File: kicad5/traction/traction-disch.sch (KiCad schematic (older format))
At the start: 26 parts

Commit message: Rev A.7: review round 7 response (RR01-RR10, A6-R01-R14) + cross-check
Two independent rechecks of c963794 were verified finding by finding and
classified in docs/review-A7-disposition.md (+ .csv): 17 confirmed and fixed,
1 spec gap closed, 3 firmware handled, 3 already-tracked release gates. Two
further defects were self-found (N10, N11).

Safety logic (control card):
- 74LVC3G17-Q100 Schmitt buffer between the RC timing nodes (clear one-shot,
  soft-off delay) and the LVC inputs they drove at 14,000-63,500 ns/V. The
  FS0B line goes through it too; a 100 k pull-down makes a dead buffer
  force DRV_EN low.
- FS0B/FS1B pull-ups 1 k -> 5.1 k (FS1B inside its 2 mA V_OL point).
- FAULT_OUT made sink-only (BAT46): a grounded vehicle wire can no longer
  preset ASC. A KL30 short is clamped at the latch.
- DRV_EN and ASC_CMD read-backs to the MCU for a boot self-test.
- Latches moved to Nexperia 74LVC1G74DC-Q100 (the TI part is not Q100).
- CCLR changed to C0G.

ASC entry is now break-before-make:
- A 12 nF delay (+ fast-release diode) holds the LS ASC off >= 3.4 us.
- MCU path: HS off via the eFlexPWM fault, then PWM-ASC with EN high.
- MCU-dead path: FS0B, then the delayed ASC.
- EN is never dropped for ASC: NSI6611 DS 8.12 honours DESAT over ASC only
  with EN high. The first draft's DASC diode did drop it and was removed
  after the cross-check.
- 1 k series resistor at each LS ASC pin.
- ASC opto LED resistor 470 -> 270 R (TLP152 I_FLH max 7.5 mA).

Gate supply:
- The flyback FB divider senses its own aux rectifier, so the start feed
  can no longer lock gate power out at high KL30.
- 52.3k/15k: VCC2 15.4 V nominal, 13.54-16.7 V corners.
- Boost output capacitors 25 V -> 50 V.

Models and checkers:
- IGBT and diode share the coldplate term.
- Flyback bank inductance corrected.
- SC soft-off checked at both I_STO corners (release gate).
- FW-06 as a measured budget: 15.6 us + 7.0 us all-off -> 905/542 V.
- bom-gen preflight and a JSWD pin-count check (Samtec 10-pin).
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
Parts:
- removed JCTL: HDR-1x4-2.54, HDR1x4, symbol traction-r1:HDR-1x4-2.54
- removed JDCN, JDCP: STUD-M6, StudM6, symbol traction-r1:TERM_1
- removed RBLD1, RBLD10, RBLD11, RBLD12, RBLD2, RBLD3, RBLD4, RBLD5: 22k, R2512, symbol traction-r1:R
- added CQD: 100nF, C0603, symbol traction-r1:C
- added PSQD: QA01C-18, SIP7, symbol traction-r1:QA01C-18
- added QDIS: HCM75S12T4K3, TO247-4L, symbol traction-r1:HCM75S12T4K3
- added RDIS1, RDIS2, RDIS3, RDIS4: 470R, AxialWW10W, symbol traction-r1:R
- added RQDG: 47R, R0603, symbol traction-r1:R
- added RQDL: 470R, R0603, symbol traction-r1:R
- added RQDPD: 10k, R0603, symbol traction-r1:R
- added UQD: TLP152, SO6, symbol traction-r1:TLP152
- JCTL: renamed from RBLD6; value 22k -> HDR-1x4-2.54; footprint R2512 -> HDR1x4; symbol traction-r1:R -> traction-r1:HDR-1x4-2.54; MPN R2512-22k-2W -> HDR-1x4-2.54
- JDCN: renamed from RBLD7; value 22k -> STUD-M6; footprint R2512 -> StudM6; symbol traction-r1:R -> traction-r1:TERM_1; MPN R2512-22k-2W -> STUD-M6
- JDCP: renamed from RBLD8; value 22k -> STUD-M6; footprint R2512 -> StudM6; symbol traction-r1:R -> traction-r1:TERM_1; MPN R2512-22k-2W -> STUD-M6
- RBLD10: renamed from PSQD; value QA01C-18 -> 22k; footprint SIP7 -> R2512; symbol traction-r1:QA01C-18 -> traction-r1:R; MPN QA01C-18 -> R2512-22k-2W
- RBLD11: renamed from QDIS; value HCM75S12T4K3 -> 22k; footprint TO247-4L -> R2512; symbol traction-r1:HCM75S12T4K3 -> traction-r1:R; MPN HCM75S12T4K3 -> R2512-22k-2W
- RBLD12: renamed from UQD; value TLP152 -> 22k; footprint SO6 -> R2512; symbol traction-r1:TLP152 -> traction-r1:R; LCSC C17255258 -> CLASS; MPN TLP152 -> R2512-22k-2W
- RBLD2: renamed from CQD; value 100nF -> 22k; footprint C0603 -> R2512; symbol traction-r1:C -> traction-r1:R; MPN MLCC-100nF-25V -> R2512-22k-2W
- RBLD3: renamed from RDIS1; value 470R -> 22k; footprint AxialWW10W -> R2512; MPN WW-470R-10W-AX -> R2512-22k-2W
- RBLD4: renamed from RDIS2; value 470R -> 22k; footprint AxialWW10W -> R2512; MPN WW-470R-10W-AX -> R2512-22k-2W
- RBLD5: renamed from RDIS3; value 470R -> 22k; footprint AxialWW10W -> R2512; MPN WW-470R-10W-AX -> R2512-22k-2W
- RBLD6: renamed from RDIS4; value 470R -> 22k; footprint AxialWW10W -> R2512; MPN WW-470R-10W-AX -> R2512-22k-2W
- RBLD7: renamed from RQDG; value 47R -> 22k; footprint R0603 -> R2512; MPN R0603-47R -> R2512-22k-2W
- RBLD8: renamed from RQDL; value 470R -> 22k; footprint R0603 -> R2512; MPN R0603-470R -> R2512-22k-2W
- RBLD9: renamed from RQDPD; value 10k -> 22k; footprint R0603 -> R2512; MPN R0603-10k -> R2512-22k-2W
- renumbered RBLD9 to RBLD1
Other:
- note added: "220 kW pk Discharge (HV, bolt-on) - 3 of 4 · rev A.7 · 3 sections · 26 components"
- note removed: "220 kW pk Discharge (HV, bolt-on) - 3 of 4 · rev A.6 · 3 sections · 26 components"
- moved on the sheet: RBLD1, RBLD3, RBLD4, RBLD5, RBLD6, RBLD7, RBLD8, RBLD9
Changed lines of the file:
@@
 Title "Traction Inverter — Discharge board (bolt-on, XM3 pattern)"
 Date "2026-09-23"
-Rev "A.6"
+Rev "A.7"
 Comp "Traction Inverter 220 kW pk - Discharge (HV, bolt-on), sheet 3 of 4"
 Comment1 "Inverter = Power board + Cap bank busbar + bolt-on Discharge board (all HV) + Control card (LV); safe state holds with any link lost"
@@
 $EndDescr
 Text Notes 600 7600 0    60   ~ 12
-220 kW pk Discharge (HV, bolt-on) - 3 of 4   ·   rev A.6   ·   3 sections   ·   26 components
+220 kW pk Discharge (HV, bolt-on) - 3 of 4   ·   rev A.7   ·   3 sections   ·   26 components
 Text Notes 600 7900 0    50   ~ 0
 NET NAMING: U<ref>_<PIN> = node at that IC pin   ·   R<stem>_M = series-pair midpoint   ·   R<stem>_<nm> = tap between R<stem>n/m   ·   all others are explicit design nets   ·   same name on another sheet = same net, joined only at the named connector/stud/tab
@@
 $Comp
 L traction-r1:HDR-1x4-2.54 JCTL
-U 1 1 5E000142
+U 1 1 5E00014D
 P 9150 5850
 F 0 "JCTL" H 8750 5550 50  0000 R CNN
@@
 $Comp
 L traction-r1:TERM_1 JDCN
-U 1 1 5E000143
+U 1 1 5E00014E
 P 8800 5300
 F 0 "JDCN" H 8800 5140 50  0000 C CNN
@@
 $Comp
 L traction-r1:TERM_1 JDCP
-U 1 1 5E000144
+U 1 1 5E00014F
 P 8800 4900
 F 0 "JDCP" H 8800 4740 50  0000 C CNN
@@
 $Comp
 L traction-r1:R RBLD1
-U 1 1 5E000145
+U 1 1 5E000150
 P 8300 1150
 F 0 "RBLD1" H 8300 990 50  0000 C CNN
@@
 $Comp
 L traction-r1:R RBLD10
-U 1 1 5E000146
+U 1 1 5E000151
 P 9800 2350
 F 0 "RBLD10" H 9800 2190 50  0000 C CNN
@@
 $Comp
 L traction-r1:R RBLD11
-U 1 1 5E000147
+U 1 1 5E000152
 P 9800 2750
 F 0 "RBLD11" H 9800 2590 50  0000 C CNN
@@
 $Comp
 L traction-r1:R RBLD12
-U 1 1 5E000148
+U 1 1 5E000153
 P 9800 3150
 F 0 "RBLD12" H 9800 2990 50  0000 C CNN
@@
 $Comp
 L traction-r1:R RBLD2
-U 1 1 5E000149
+U 1 1 5E000154
 P 8300 1550
 F 0 "RBLD2" H 8300 1390 50  0000 C CNN
@@
 $Comp
 L traction-r1:R RBLD3
-U 1 1 5E00014A
+U 1 1 5E000155
 P 8300 1950
 F 0 "RBLD3" H 8300 1790 50  0000 C CNN
@@
 $Comp
 L traction-r1:R RBLD4
-U 1 1 5E00014B
+U 1 1 5E000156
 P 8300 2350
 F 0 "RBLD4" H 8300 2190 50  0000 C CNN
@@
 $Comp
 L traction-r1:R RBLD5
-U 1 1 5E00014C
+U 1 1 5E000157
 P 8300 2750
 F 0 "RBLD5" H 8300 2590 50  0000 C CNN
@@
 $Comp
 L traction-r1:R RBLD6
-U 1 1 5E00014D
+U 1 1 5E000158
 P 8300 3150
 F 0 "RBLD6" H 8300 2990 50  0000 C CNN
@@
 $Comp
 L traction-r1:R RBLD7
-U 1 1 5E00014E
+U 1 1 5E000159
 P 9800 1150
 F 0 "RBLD7" H 9800 990 50  0000 C CNN
@@
 $Comp
 L traction-r1:R RBLD8
-U 1 1 5E00014F
+U 1 1 5E00015A
 P 9800 1550
 F 0 "RBLD8" H 9800 1390 50  0000 C CNN
@@
 $Comp
 L traction-r1:R RBLD9
-U 1 1 5E000150
+U 1 1 5E00015B
 P 9800 1950
 F 0 "RBLD9" H 9800 1790 50  0000 C CNN
@@
 $Comp
 L traction-r1:QA01C-18 PSQD
-U 1 1 5E000151
+U 1 1 5E00015C
 P 2850 1800
 F 0 "PSQD" H 2450 1500 50  0000 R CNN
@@
 $Comp
 L traction-r1:HCM75S12T4K3 QDIS
-U 1 1 5E000152
+U 1 1 5E00015D
 P 4850 1350
 F 0 "QDIS" H 4450 1000 50  0000 R CNN
@@
 $Comp
 L traction-r1:TLP152 UQD
-U 1 1 5E000153
+U 1 1 5E00015E
 P 2850 3550
 F 0 "UQD" H 2450 3250 50  0000 R CNN
@@
 $Comp
 L traction-r1:C CQD
-U 1 1 5E000154
+U 1 1 5E00015F
 P 2650 5850
 F 0 "CQD" H 2650 5690 50  0000 C CNN
@@
 $Comp
 L traction-r1:R RDIS1
-U 1 1 5E000155
+U 1 1 5E000160
 P 4650 2000
 F 0 "RDIS1" H 4650 1840 50  0000 C CNN
@@
 $Comp
 L traction-r1:R RDIS2
-U 1 1 5E000156
+U 1 1 5E000161
 P 4650 2400
 F 0 "RDIS2" H 4650 2240 50  0000 C CNN
@@
 $Comp
 L traction-r1:R RDIS3
-U 1 1 5E000157
+U 1 1 5E000162
 P 4650 2800
 F 0 "RDIS3" H 4650 2640 50  0000 C CNN
@@
 $Comp
 L traction-r1:R RDIS4
-U 1 1 5E000158
+U 1 1 5E000163
 P 4650 3200
 F 0 "RDIS4" H 4650 3040 50  0000 C CNN
@@
 $Comp
 L traction-r1:R RQDG
-U 1 1 5E000159
+U 1 1 5E000164
 P 2650 5050
 F 0 "RQDG" H 2650 4890 50  0000 C CNN
@@
 $Comp
 L traction-r1:R RQDL
-U 1 1 5E00015A
+U 1 1 5E000165
 P 2650 4650
 F 0 "RQDL" H 2650 4490 50  0000 C CNN
@@
 $Comp
 L traction-r1:R RQDPD
-U 1 1 5E00015B
+U 1 1 5E000166
 P 2650 5450
 F 0 "RQDPD" H 2650 5290 50  0000 C CNN

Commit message: Rev A.8: review round 8 response (R7-01..07, A7-N01..05) + cross-check
Review round 8 on 2ac42ed, every finding verified and classified in
docs/review-A8-disposition.md (+ .csv); findings log F90-F105.

Hardware (+Rs18/unit: SiC Rs71,040, IGBT Rs45,540):
- UASCG 74LVC1G08-Q100: ASC_CMD = ASC latch AND no driver FLT, so a
  latched DESAT drops ASC on every path, FS1B included (R7-01/A7-N01;
  NSI6611 DS Fig. 8.11 read directly)
- USCH2 74LVC3G17-Q100 buffers both latch presets and drives QDIS_CMD;
  FLT diode-OR now BAT46 for the Schmitt threshold (R7-02, R7-03, N12)
- ZSET BZT52-B5V6 to ground replaces the clamp into V5A; RENP2 removed
  (A7-N04; B5V6 keeps a 35 V load dump under the 6.5 V V_I abs max)
- RASCL = RQDL = 261 R: both TLP152 LEDs 10.3-14.8 mA, inside 10-15 mA
- dead-state pulls: RFCB on FLT_CMB_B, RASCP moved to ASC_Q
- CFLTF2 100 pF on FLT_LS_N; discharge header V15-GND-CMD-GND

Firmware contract: FW-15 always clears the ASC latch; FW-16 runs on
measured no-HV/standstill conditions (stored-pass arming otherwise),
handles the FS_GPIO1 flyback OR and injects FLT from the MCU pins;
FW-08b; FS1B_TDELAY = 0, TDUR = 100 ms; FAULT_OUT outcomes stated.

Tooling: ERC locks by net, pin number and first-match MPN per SKU
(864 checks, each new one mutation-tested); computed judges replace
fixed PASS rows; S4 static junction path + static-plate bound; VCC2
FB-sense per corner; bom-gen publishes atomically, rounds ext prices.

Gates: pins 1782/1782, ERC 864/0, design-verify 108P/14W/0F,
sim-verify 23P/6W/0F, marine 81P/19W/0F.

Co-Authored-By: Claude Opus 5.5 <noreply@anthropic.com>
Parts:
- RQDL: value 470R -> 261R; MPN R0603-470R -> R0603-261R-1%
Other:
- note added: "220 kW pk Discharge (HV, bolt-on) - 3 of 4 · rev A.8 · 3 sections · 26 components"
- note removed: "220 kW pk Discharge (HV, bolt-on) - 3 of 4 · rev A.7 · 3 sections · 26 components"
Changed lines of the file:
@@
 Title "Traction Inverter — Discharge board (bolt-on, XM3 pattern)"
 Date "2026-09-23"
-Rev "A.7"
+Rev "A.8"
 Comp "Traction Inverter 220 kW pk - Discharge (HV, bolt-on), sheet 3 of 4"
 Comment1 "Inverter = Power board + Cap bank busbar + bolt-on Discharge board (all HV) + Control card (LV); safe state holds with any link lost"
@@
 $EndDescr
 Text Notes 600 7600 0    60   ~ 12
-220 kW pk Discharge (HV, bolt-on) - 3 of 4   ·   rev A.7   ·   3 sections   ·   26 components
+220 kW pk Discharge (HV, bolt-on) - 3 of 4   ·   rev A.8   ·   3 sections   ·   26 components
 Text Notes 600 7900 0    50   ~ 0
 NET NAMING: U<ref>_<PIN> = node at that IC pin   ·   R<stem>_M = series-pair midpoint   ·   R<stem>_<nm> = tap between R<stem>n/m   ·   all others are explicit design nets   ·   same name on another sheet = same net, joined only at the named connector/stud/tab
@@
 P 2650 4650
 F 0 "RQDL" H 2650 4490 50  0000 C CNN
-F 1 "470R" H 2650 4820 50  0000 C CNN
+F 1 "261R" H 2650 4820 50  0000 C CNN
 F 2 "R0603" H 2650 4650 50  0001 C CNN
 F 3 "~" H 2650 4650 50  0001 C CNN
 F 4 "CLASS" H 2650 4650 50  0001 C CNN "LCSC"
-F 5 "R0603-470R" H 2650 4650 50  0001 C CNN "MPN"
+F 5 "R0603-261R-1%" H 2650 4650 50  0001 C CNN "MPN"
 	1    2650 4650
 	1    0    0    -1

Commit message: Rev A.9: review round 9 response (A8-01..03, A8-N01..N03) + cross-check
Review round 9 on 0da9014, every finding verified and classified in
docs/review-A9-disposition.md (+ .csv, 34 items); findings log F106-F119.

Hardware (+Rs29/unit: SiC Rs71,069, IGBT Rs45,569):
- PSASC/PSQD bound to the real QA01C-18 sheet (+18/-3 V; F61 had read
  the base QA01C, +20/-4 V): envelope 16.9-20.9 V, ASC entry 7.52 us,
  FW-06 end-point 906 V; discharge gate divider RQDG 1.5k (Vgs 13.4-18.1 V)
- FLT/RDY pull-ups and the diode-OR pull-up moved to V5GD (the drivers'
  VCC1; FLT/RDY abs max = VCC1), V5GD read by the MCU on PTB5
- HARNESS40 re-laid: VBAT and V5GD touch only ground in both row-by-row
  and odd/even dual-row numbering; connector family chosen at layout
- self-found: the power board's LV side ran on unswitched KL30
  (~150 mA parked) - card-side P-FET switch DMP6023LEQ on V5A with a
  slew network; resolver LDO enabled by V5A; parking drain <= 43 uA
- RFS4 = ROHM ESR03 anti-surge; CASC/CQD 50 V

Firmware contract: FW-16 energy-limited eligibility (read < 3 V or QDIS
for 2 tau); V_DC invalid while V5GD is out of window; DESATs to NVM;
BACKUP_SAFETY_PATH_FS1B = 0; motor/vehicle release rule for SPO energy.

Gates: pins 1804/1804, ERC 883/0 (new locks mutation-tested),
design-verify 116P/14W/0F, sim-verify 23P/6W/0F, marine 81P/19W/0F.

Co-Authored-By: Claude Opus 5.5 <noreply@anthropic.com>
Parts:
- CQD: MPN MLCC-100nF-25V -> MLCC-100nF-50V
- RQDG: value 47R -> 1.5k; MPN R0603-47R -> R0603-1k5
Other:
- note added: "220 kW pk Discharge (HV, bolt-on) - 3 of 4 · rev A.9 · 3 sections · 26 components"
- note removed: "220 kW pk Discharge (HV, bolt-on) - 3 of 4 · rev A.8 · 3 sections · 26 components"
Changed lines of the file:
@@
 Title "Traction Inverter — Discharge board (bolt-on, XM3 pattern)"
 Date "2026-09-23"
-Rev "A.8"
+Rev "A.9"
 Comp "Traction Inverter 220 kW pk - Discharge (HV, bolt-on), sheet 3 of 4"
 Comment1 "Inverter = Power board + Cap bank busbar + bolt-on Discharge board (all HV) + Control card (LV); safe state holds with any link lost"
@@
 $EndDescr
 Text Notes 600 7600 0    60   ~ 12
-220 kW pk Discharge (HV, bolt-on) - 3 of 4   ·   rev A.8   ·   3 sections   ·   26 components
+220 kW pk Discharge (HV, bolt-on) - 3 of 4   ·   rev A.9   ·   3 sections   ·   26 components
 Text Notes 600 7900 0    50   ~ 0
 NET NAMING: U<ref>_<PIN> = node at that IC pin   ·   R<stem>_M = series-pair midpoint   ·   R<stem>_<nm> = tap between R<stem>n/m   ·   all others are explicit design nets   ·   same name on another sheet = same net, joined only at the named connector/stud/tab
@@
 F 3 "~" H 2650 5850 50  0001 C CNN
 F 4 "CLASS" H 2650 5850 50  0001 C CNN "LCSC"
-F 5 "MLCC-100nF-25V" H 2650 5850 50  0001 C CNN "MPN"
+F 5 "MLCC-100nF-50V" H 2650 5850 50  0001 C CNN "MPN"
 	1    2650 5850
 	1    0    0    -1
@@
 P 2650 5050
 F 0 "RQDG" H 2650 4890 50  0000 C CNN
-F 1 "47R" H 2650 5220 50  0000 C CNN
+F 1 "1.5k" H 2650 5220 50  0000 C CNN
 F 2 "R0603" H 2650 5050 50  0001 C CNN
 F 3 "~" H 2650 5050 50  0001 C CNN
 F 4 "CLASS" H 2650 5050 50  0001 C CNN "LCSC"
-F 5 "R0603-47R" H 2650 5050 50  0001 C CNN "MPN"
+F 5 "R0603-1k5" H 2650 5050 50  0001 C CNN "MPN"
 	1    2650 5050
 	1    0    0    -1

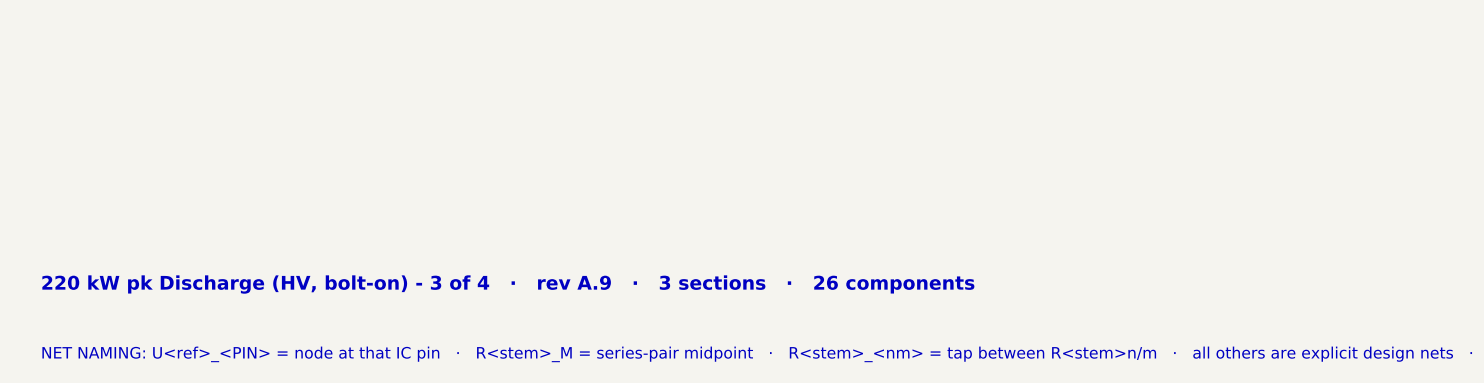
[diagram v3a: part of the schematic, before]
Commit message: Rev A.10: schematic rechecks of A.9 (A9-S01, S9-01, S9-02)
Two schematic-only rechecks of 7235337 kept every A.9 correction;
dispositioned in docs/review-A10-disposition.md (+ .csv); F120-F122.

- RDY_HS/RDY_LS now reach UAND1/UAND2 through a third 74LVC3G17-Q100
  (USCH3, RRDB dead-state pull-down): the open-drain lines rose at
  ~20-100 ns/V against the 74LVC1G11's 10 ns/V limit (A9-S01; reverses
  the round-7/8 "state-benign" rejection)
- RASCG = ROHM ESR03EZPF2201 (0.27 W at 85 C): it carries up to 0.12 W
  for as long as ASC is held; 2.2 k kept for the ASC timing (S9-01)
- discharge sheet note 66k bleeder; gate divider stated as 13.3-18.2 V
  (a divider, not a clamp); A9 disposition quotes the final harness map

+Rs11/unit (SiC Rs71,080, IGBT Rs45,580).
Gates: pins 1815/1815, ERC 891/0 (new locks mutation-tested),
design-verify 118P/14W/0F, sim-verify 23P/6W/0F, marine 81P/19W/0F.

Co-Authored-By: Claude Opus 5.5 <noreply@anthropic.com>
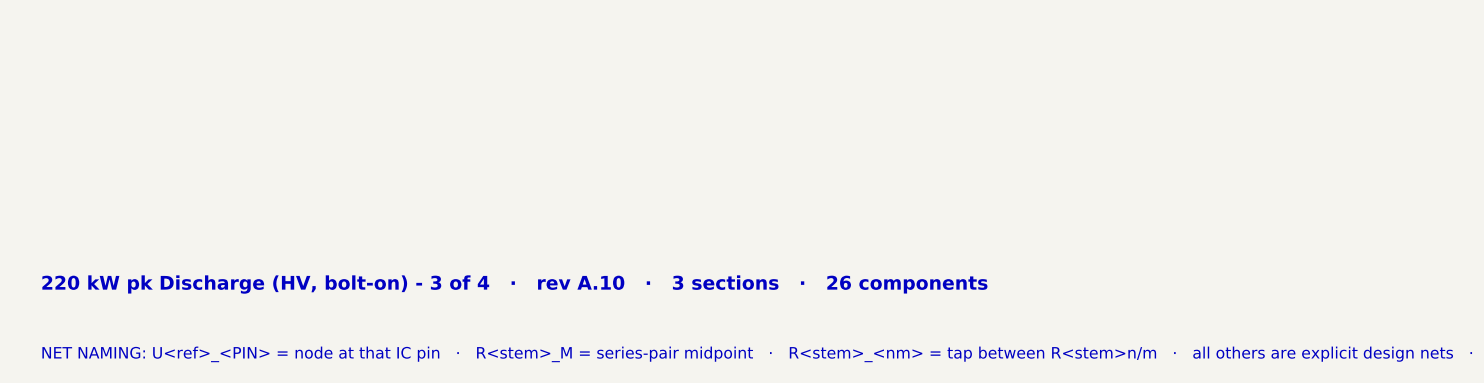
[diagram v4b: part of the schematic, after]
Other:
- note added: "220 kW pk Discharge (HV, bolt-on) - 3 of 4 · rev A.10 · 3 sections · 26 components"
- note removed: "220 kW pk Discharge (HV, bolt-on) - 3 of 4 · rev A.9 · 3 sections · 26 components"
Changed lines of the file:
@@
 Title "Traction Inverter — Discharge board (bolt-on, XM3 pattern)"
 Date "2026-09-23"
-Rev "A.9"
+Rev "A.10"
 Comp "Traction Inverter 220 kW pk - Discharge (HV, bolt-on), sheet 3 of 4"
 Comment1 "Inverter = Power board + Cap bank busbar + bolt-on Discharge board (all HV) + Control card (LV); safe state holds with any link lost"
-Comment2 "Content: passive 67.5k bleeder (58 s) + commanded active path (1.88k, 1.6 s) — NEVER energize without this board fitted"
+Comment2 "Content: passive 66k bleeder (56 s nom / 65 s worst) + commanded active path (1.88k, 1.6 s) — NEVER energize without this board fitted"
 Comment3 "3 functional sections - 26 components - cross-section links are net labels; wires are pin stubs only"
 Comment4 "Every component carries MPN + LCSC fields (CLASS = buy to class spec, ALT footprint-compatible second source in BOM)"
 $EndDescr
 Text Notes 600 7600 0    60   ~ 12
-220 kW pk Discharge (HV, bolt-on) - 3 of 4   ·   rev A.9   ·   3 sections   ·   26 components
+220 kW pk Discharge (HV, bolt-on) - 3 of 4   ·   rev A.10   ·   3 sections   ·   26 components
 Text Notes 600 7900 0    50   ~ 0
 NET NAMING: U<ref>_<PIN> = node at that IC pin   ·   R<stem>_M = series-pair midpoint   ·   R<stem>_<nm> = tap between R<stem>n/m   ·   all others are explicit design nets   ·   same name on another sheet = same net, joined only at the named connector/stud/tab
